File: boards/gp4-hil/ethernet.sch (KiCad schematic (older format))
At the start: 65 parts, among them J1 BEL_FUSE_0826-1G1T-23-F, J3 XILINX_JTAG_ICESIDE, J4 XILINX_JTAG_ICESIDE, U2 XC7A100T-1FTG256C, U29 TXB0104RUT, U30 TXB0104RUT, U33 125 MHz, U5 KSZ9031RN, U7 25 MHz

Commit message: Finished Ethernet layout
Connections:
- net 2V5: no longer C13.1, C2.1, C8.1
- net A2V5_ETH: now also C13.1, C2.1, C8.1
- net ETH_B_N: now also J1.4 (CH2_P); no longer J1.5 (CH2_N)
- net ETH_B_P: now also J1.5 (CH2_N); no longer J1.4 (CH2_P)
- net ETH_D_N: now also J1.8 (CH4_P); no longer J1.9 (CH4_N)
- net ETH_D_P: now also J1.9 (CH4_N); no longer J1.8 (CH4_P)
- net FPGA_CLK_125MHZ: now also U2.N11 (IO_L13P_T2_MRCC_14); no longer U2.N14 (IO_L12P_T1_MRCC_14)
- net PHY_INT_N: now also U2.P13 (IO_L11N_T1_SRCC_14); no longer U2.K13 (IO_L5P_T0_D06_14)
- net PHY_MDC: now also U2.P14 (IO_L12N_T1_MRCC_14); no longer U2.T13 (IO_L16N_T2_A15_D31_14)
- net PHY_MDIO: now also U2.N13 (IO_L11P_T1_SRCC_14); no longer U2.P11 (IO_L14N_T2_SRCC_14)
- net RGMII_RXC: now also U2.N14 (IO_L12P_T1_MRCC_14); no longer U2.N11 (IO_L13P_T2_MRCC_14)
- net RGMII_RXD0: now also U2.T13 (IO_L16N_T2_A15_D31_14); no longer U2.P10 (IO_L14P_T2_SRCC_14)
- net RGMII_RXD1: now also U2.R13 (IO_L16P_T2_CSI_B_14); no longer U2.N13 (IO_L11P_T1_SRCC_14)
- net RGMII_RXD2: now also U2.T14 (IO_L10P_T1_D14_14); no longer U2.T15 (IO_L10N_T1_D15_14)
- net RGMII_RXD3: now also U2.T15 (IO_L10N_T1_D15_14); no longer U2.T14 (IO_L10P_T1_D14_14)
- net RGMII_RX_DV: now also U2.R12 (IO_L15P_T2_DQS_RDWR_B_14); no longer U2.P13 (IO_L11N_T1_SRCC_14)
- net VDD1_1V8_EN: now also U2.K13 (IO_L5P_T0_D06_14); no longer U2.R12 (IO_L15P_T2_DQS_RDWR_B_14)
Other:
- note added: "Swap P/N for routability.\nKSZ9031 can auto compensate for this\nNo register settings required"
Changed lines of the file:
@@
 Sheet 3 7
 Title "GreenPak Hardware-In-Loop Test Platform"
-Date "2016-05-23"
+Date "2016-05-24"
 Rev "0.1"
 Comp "Andrew Zonenberg"
@@
 	-1   0    0    -1
 $EndComp
-Text HLabel 1150 800  0    60   Input ~ 0
+Text HLabel 6800 6450 0    60   Input ~ 0
 2V5
 Text HLabel 1150 1300 0    60   Input ~ 0
@@
 Text Label 1800 9000 0    60   ~ 0
 ETH_A_P
-Text Label 1800 9400 0    60   ~ 0
+Text Label 1800 9600 0    60   ~ 0
 ETH_B_P
 Text Label 1800 9800 0    60   ~ 0
 ETH_C_P
-Text Label 1800 10200 0    60   ~ 0
+Text Label 1800 10400 0    60   ~ 0
 ETH_D_P
 Text Label 1800 10600 0    60   ~ 0
@@
 Text Label 1800 9200 0    60   ~ 0
 ETH_A_N
-Text Label 1800 9600 0    60   ~ 0
+Text Label 1800 9400 0    60   ~ 0
 ETH_B_N
 Text Label 1800 10000 0    60   ~ 0
 ETH_C_N
-Text Label 1800 10400 0    60   ~ 0
+Text Label 1800 10200 0    60   ~ 0
 ETH_D_N
 Text Notes 1150 3250 0    60   ~ 0
@@
 Text Label 8400 11050 2    60   ~ 0
 1V8
+Text Label 16000 7000 2    60   ~ 0
+RGMII_RXD3
 Text Label 16000 6900 2    60   ~ 0
-RGMII_RXD3
-Text Label 16000 7000 2    60   ~ 0
 RGMII_RXD2
+Text Label 16000 8100 2    60   ~ 0
+RGMII_RXD1
+Text Label 16000 8200 2    60   ~ 0
+RGMII_RXD0
+Text Label 16000 7900 2    60   ~ 0
+RGMII_RX_DV
+Text Label 16000 7300 2    60   ~ 0
+RGMII_RXC
+Text Label 16000 7400 2    60   ~ 0
+PHY_MDC
 Text Label 16000 7100 2    60   ~ 0
-RGMII_RXD1
-Text Label 16000 7700 2    60   ~ 0
-RGMII_RXD0
+PHY_MDIO
 Text Label 16000 7200 2    60   ~ 0
-RGMII_RX_DV
-Text Label 16000 7500 2    60   ~ 0
-RGMII_RXC
-Text Label 16000 8200 2    60   ~ 0
-PHY_MDC
-Text Label 16000 7800 2    60   ~ 0
-PHY_MDIO
-Text Label 16000 5900 2    60   ~ 0
 PHY_INT_N
 Text Label 16000 6300 2    60   ~ 0
@@
 Text HLabel 16000 8000 0    60   Output ~ 0
 VDD1_2V5_EN
-Text HLabel 16000 7900 0    60   Output ~ 0
+Text HLabel 16000 5900 0    60   Output ~ 0
 VDD1_1V8_EN
 Text HLabel 16050 5800 0    60   Output ~ 0
@@
 	16000 7200 16200 7200
 Wire Wire Line
-	16200 7100 16000 7100
-Wire Wire Line
 	16000 6300 16200 6300
 Wire Wire Line
@@
 	16000 6000 16200 6000
 Wire Wire Line
-	16000 7700 16200 7700
+	16000 7400 16200 7400
 Wire Wire Line
 	16000 8200 16200 8200
@@
 	16200 7900 16000 7900
 Wire Wire Line
-	16000 7800 16200 7800
+	16000 7100 16200 7100
 Wire Wire Line
 	15100 5500 15050 5500
@@
 Connection ~ 8850 12050
 Connection ~ 8500 11950
-Text Label 16000 7300 2    60   ~ 0
+Text Label 16000 7500 2    60   ~ 0
 FPGA_CLK_125MHZ
 Wire Wire Line
@@
 Wire Wire Line
 	16000 8500 16200 8500
-NoConn ~ 16200 7400
 $Comp
 L INDUCTOR_PWROUT L13
@@
 	0    1    1    0
 $EndComp
-Text Label 6800 6450 2    60   ~ 0
-2V5
 $Comp
 L C C179
@@
 Wire Wire Line
 	16200 6700 16000 6700
-NoConn ~ 16200 8100
+Wire Wire Line
+	16000 8100 16200 8100
+Text Label 1150 800  2    60   ~ 0
+A2V5_ETH
+NoConn ~ 16200 7700
+NoConn ~ 16200 7800
+Text Notes 2400 10550 0    60   ~ 0
+Swap P/N for routability.\nKSZ9031 can auto compensate for this\nNo register settings required
 $EndSCHEMATC

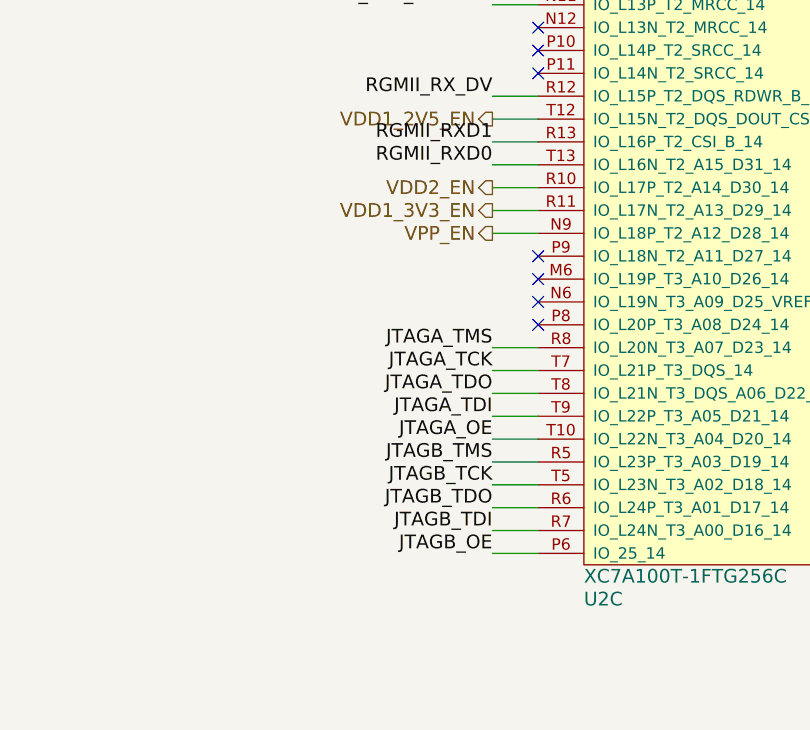
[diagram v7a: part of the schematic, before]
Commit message: More JTAG/config stuff
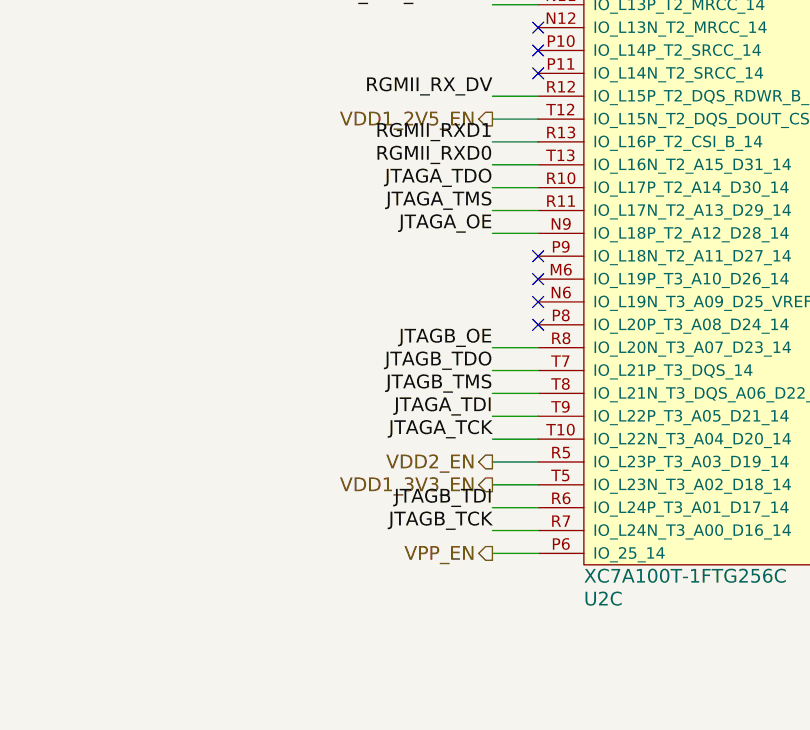
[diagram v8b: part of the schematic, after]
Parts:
- TP22, TP23: footprint azonenberg_pcb:TESTPOINT_SMT_KEYSTONE_5016 -> azonenberg_pcb:TESTPOINT_SMT_0.5MM
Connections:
- net JTAGA_OE: now also U2.N9 (IO_L18P_T2_A12_D28_14); no longer U2.T10 (IO_L22N_T3_A04_D20_14)
- net JTAGA_TCK: now also U2.T10 (IO_L22N_T3_A04_D20_14); no longer U2.T7 (IO_L21P_T3_DQS_14)
- net JTAGA_TDO: now also U2.R10 (IO_L17P_T2_A14_D30_14); no longer U2.T8 (IO_L21N_T3_DQS_A06_D22_14)
- net JTAGA_TMS: now also U2.R11 (IO_L17N_T2_A13_D29_14); no longer U2.R8 (IO_L20N_T3_A07_D23_14)
- net JTAGB_OE: now also U2.R8 (IO_L20N_T3_A07_D23_14); no longer U2.P6 (IO_25_14)
- net JTAGB_TCK: now also U2.R7 (IO_L24N_T3_A00_D16_14); no longer U2.T5 (IO_L23N_T3_A02_D18_14)
- net JTAGB_TDI: now also U2.R6 (IO_L24P_T3_A01_D17_14); no longer U2.R7 (IO_L24N_T3_A00_D16_14)
- net JTAGB_TDO: now also U2.T7 (IO_L21P_T3_DQS_14); no longer U2.R6 (IO_L24P_T3_A01_D17_14)
- net JTAGB_TMS: now also U2.T8 (IO_L21N_T3_DQS_A06_D22_14); no longer U2.R5 (IO_L23P_T3_A03_D19_14)
- net VDD1_3V3_EN: now also U2.T5 (IO_L23N_T3_A02_D18_14); no longer U2.R11 (IO_L17N_T2_A13_D29_14)
- net VDD2_EN: now also U2.R5 (IO_L23P_T3_A03_D19_14); no longer U2.R10 (IO_L17P_T2_A14_D30_14)
- net VPP_EN: now also U2.P6 (IO_25_14); no longer U2.N9 (IO_L18P_T2_A12_D28_14)
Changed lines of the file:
@@
 Sheet 3 7
 Title "GreenPak Hardware-In-Loop Test Platform"
-Date "2016-05-24"
+Date "2016-05-26"
 Rev "0.1"
 Comp "Andrew Zonenberg"
@@
 FLASH_CS_N
 NoConn ~ 16200 6200
-Text HLabel 16000 8400 0    60   Output ~ 0
+Text HLabel 16000 9600 0    60   Output ~ 0
 VDD1_3V3_EN
 Text HLabel 16000 8000 0    60   Output ~ 0
@@
 Text HLabel 16050 5600 0    60   Output ~ 0
 VDD2_1V8_EN
-Text HLabel 16000 8500 0    60   Output ~ 0
+Text HLabel 16000 9900 0    60   Output ~ 0
 VPP_EN
 NoConn ~ 16200 7600
@@
 Text Label 16500 14300 2    60   ~ 0
 JTAGB_OE
-Text Label 16000 9000 2    60   ~ 0
+Text Label 16000 8400 2    60   ~ 0
 JTAGA_TMS
-Text Label 16000 9100 2    60   ~ 0
+Text Label 16000 9400 2    60   ~ 0
 JTAGA_TCK
-Text Label 16000 9200 2    60   ~ 0
+Text Label 16000 8300 2    60   ~ 0
 JTAGA_TDO
 Text Label 16000 9300 2    60   ~ 0
 JTAGA_TDI
-Text Label 16000 9400 2    60   ~ 0
+Text Label 16000 8500 2    60   ~ 0
 JTAGA_OE
-Text Label 16000 9500 2    60   ~ 0
+Text Label 16000 9200 2    60   ~ 0
 JTAGB_TMS
-Text Label 16000 9600 2    60   ~ 0
+Text Label 16000 9800 2    60   ~ 0
 JTAGB_TCK
+Text Label 16000 9100 2    60   ~ 0
+JTAGB_TDO
 Text Label 16000 9700 2    60   ~ 0
-JTAGB_TDO
-Text Label 16000 9800 2    60   ~ 0
 JTAGB_TDI
-Text Label 16000 9900 2    60   ~ 0
+Text Label 16000 9000 2    60   ~ 0
 JTAGB_OE
 NoConn ~ 16200 8900
@@
 	1    0    0    -1
 $EndComp
-Text HLabel 16000 8300 0    60   Output ~ 0
+Text HLabel 16000 9500 0    60   Output ~ 0
 VDD2_EN
 $Comp
@@
 F 0 "TP22" H 12078 11188 50  0000 L CNN
 F 1 "TESTPOINT" H 12078 11096 50  0000 L CNN
-F 2 "azonenberg_pcb:TESTPOINT_SMT_KEYSTONE_5016" H 12000 11150 60  0001 C CNN
+F 2 "azonenberg_pcb:TESTPOINT_SMT_0.5MM" H 12000 11150 60  0001 C CNN
 F 3 "" H 12000 11150 60  0000 C CNN
 	1    12000 11150
@@
 F 0 "TP23" H 12078 12088 50  0000 L CNN
 F 1 "TESTPOINT" H 12078 11996 50  0000 L CNN
-F 2 "azonenberg_pcb:TESTPOINT_SMT_KEYSTONE_5016" H 12000 12050 60  0001 C CNN
+F 2 "azonenberg_pcb:TESTPOINT_SMT_0.5MM" H 12000 12050 60  0001 C CNN
 F 3 "" H 12000 12050 60  0000 C CNN
 	1    12000 12050
